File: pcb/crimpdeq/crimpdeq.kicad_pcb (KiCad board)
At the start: 2 copper layers, 23 x 63.8 mm, 48 parts, among them J2 USB4105-GF-A, J3 Loadcell_Pads, J4 Power_Sense_Pads, Q1 SS8550, Q2 DMG3415U, U1 ESP32-C3-MINI-1, U2 MCP73831T-2ACI/OT, U3 HX711, U5 MAX17048G+T10, U6 SY8088

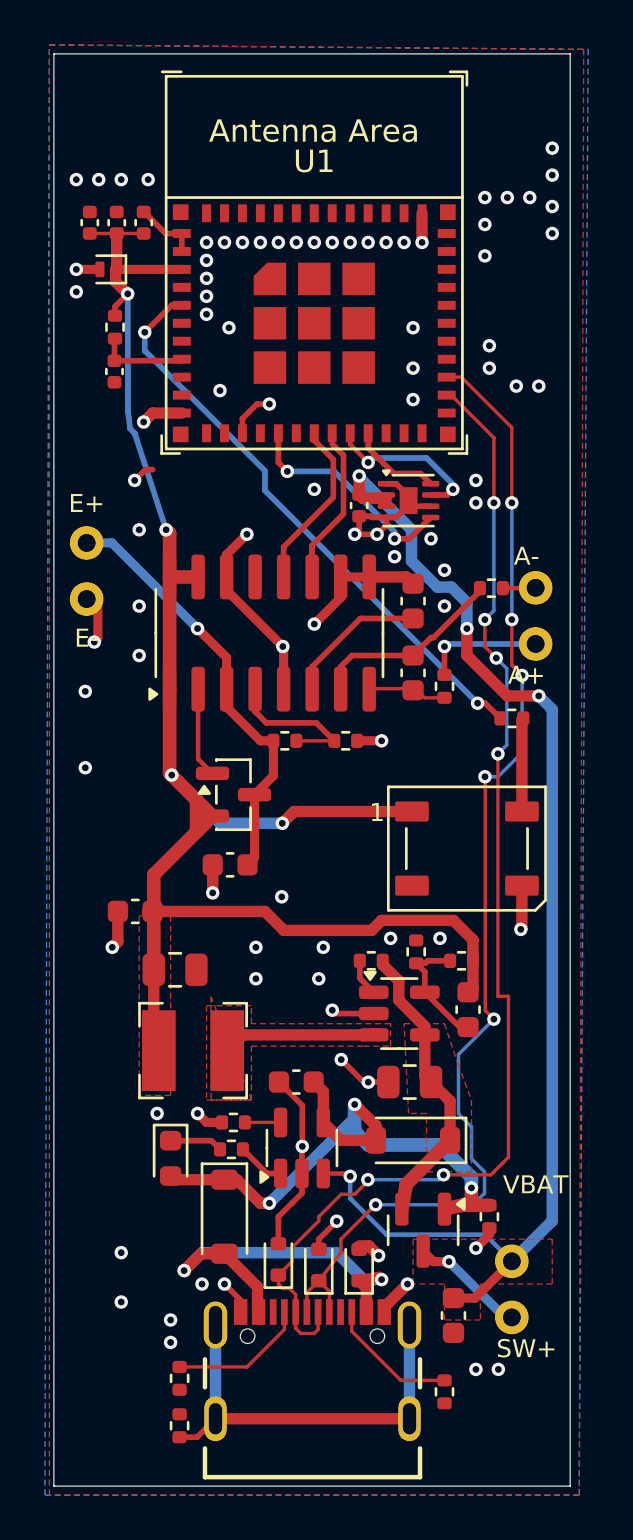
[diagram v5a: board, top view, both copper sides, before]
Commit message: feat: Fix unused tracks and cleearance violations
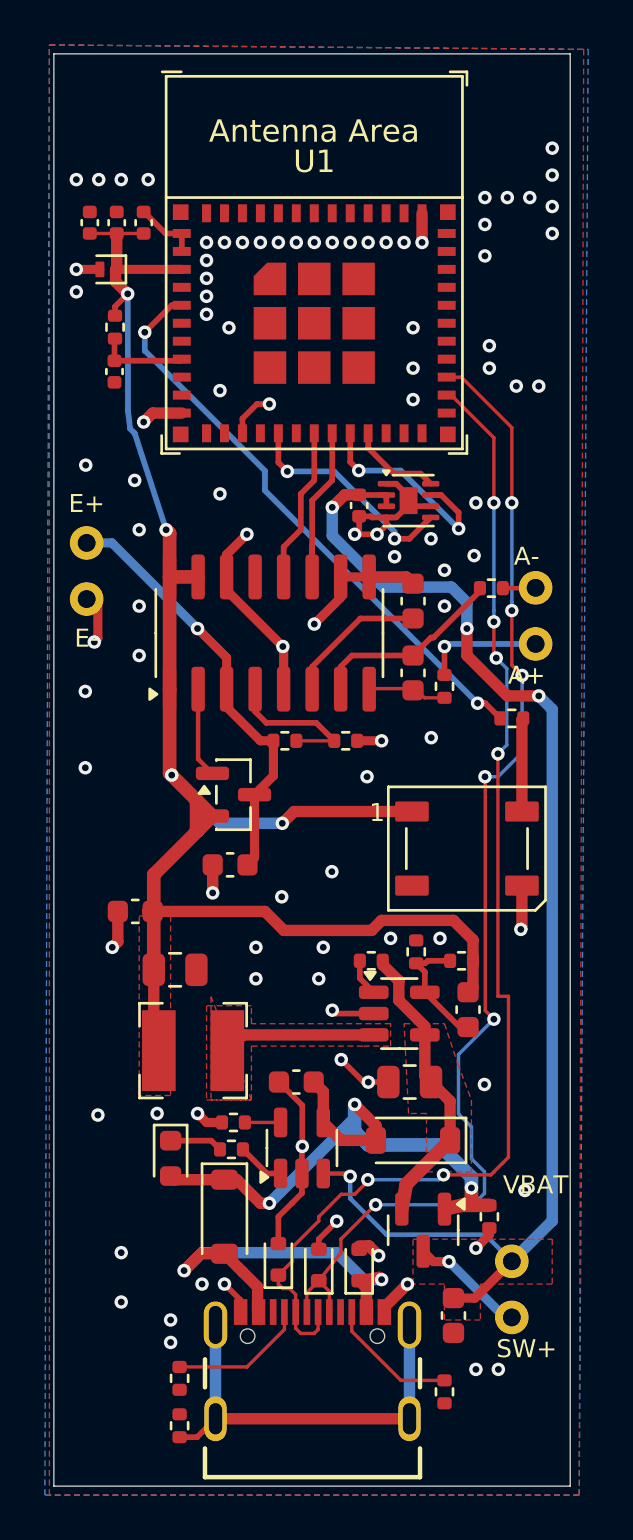
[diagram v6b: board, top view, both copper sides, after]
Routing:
- net IO6_SDA: track 7.31 -> 9.63 mm
- net GND: track 62.0 -> 61.0 mm, vias 91 -> 98
- net IO4_DATA: track 8.08 -> 7.37 mm

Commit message: feat: Simplify A+/A- routing
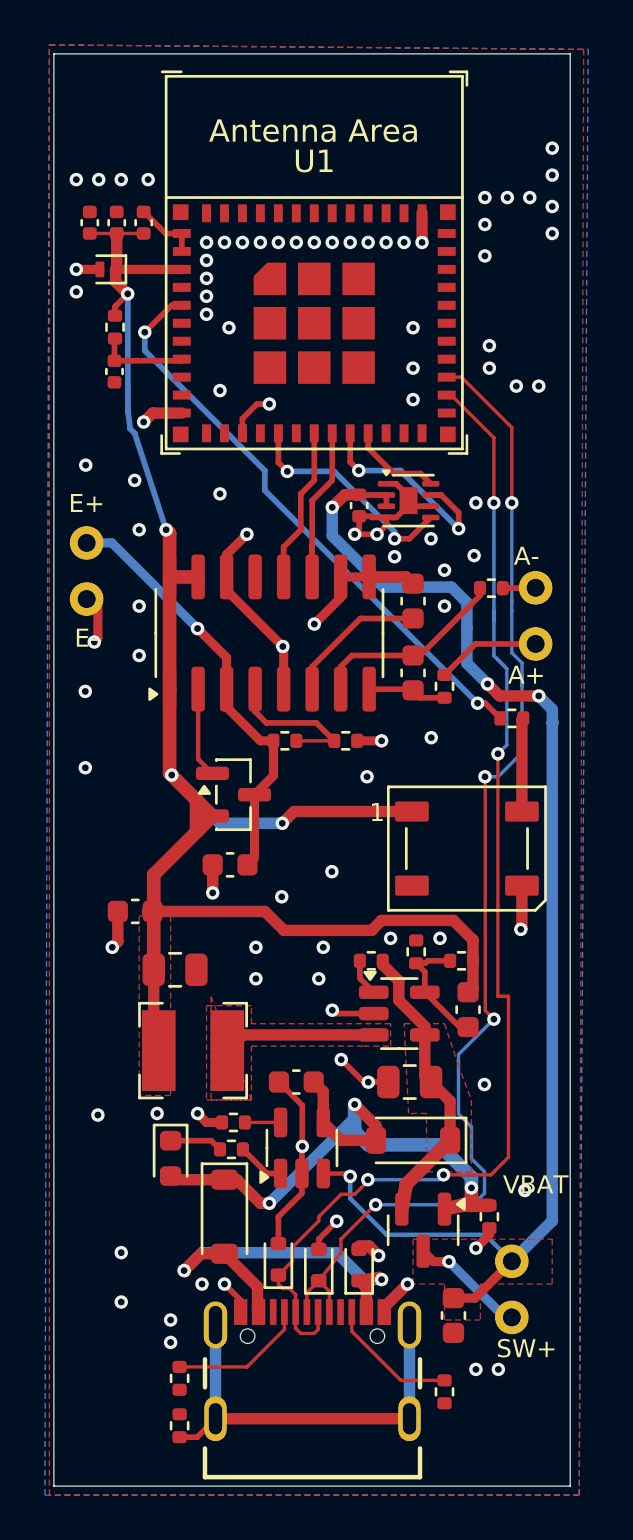
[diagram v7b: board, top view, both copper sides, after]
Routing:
- net USB_D-: track 53.6 -> 54.6 mm, vias 6 -> 4
- net A+: track 5.37 -> 4.63 mm, vias 1 -> 0
- net USB_D+: track 53.3 -> 53.7 mm, vias 6 -> 4

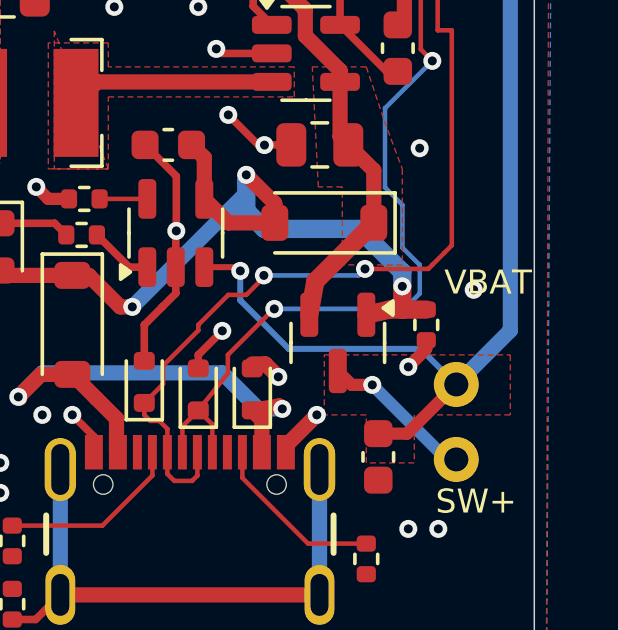
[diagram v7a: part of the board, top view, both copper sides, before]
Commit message: fix: DRC unconected GND
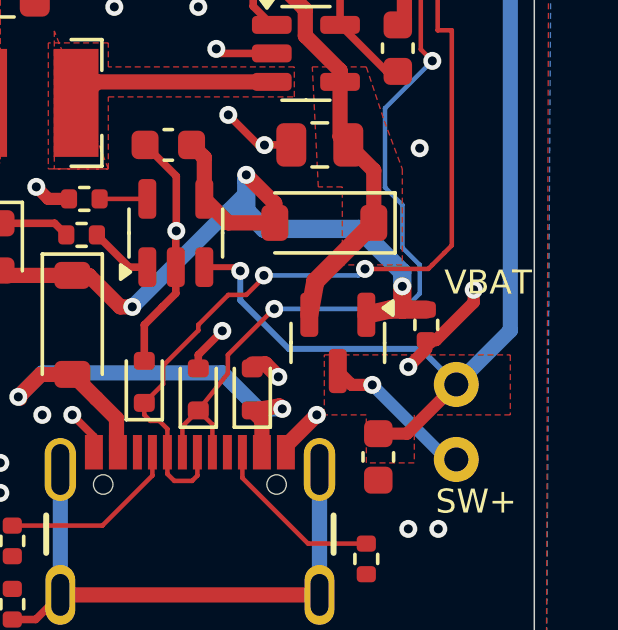
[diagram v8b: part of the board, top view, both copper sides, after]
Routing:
- net GND: track 61.0 -> 63.5 mm
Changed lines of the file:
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@@
+	)
+	(segment
+		(start 148.6 98.71)
+		(end 148.919999 98.71)
+		(width 0.4064)
+		(layer "F.Cu")
+		(net "GND")
 	)
 	(segment
@@
 	)
 	(segment
+		(start 150.18 97.449999)
+		(end 150.18 97.03)
+		(width 0.4064)
+		(layer "F.Cu")
+		(net "GND")
+	)
+	(segment
 		(start 144.0125 67.05)
 		(end 144.0125 67.3875)
@@
 		(layer "F.Cu")
 		(net "GND")
+	)
+	(segment
+		(start 148.919999 98.71)
+		(end 150.18 97.449999)
+		(width 0.4064)
+		(layer "F.Cu")
+		(net "GND")
